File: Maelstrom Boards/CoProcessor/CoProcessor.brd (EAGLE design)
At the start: 101.6 x 101.6 mm, 51 parts, among them J1 USB_MINI-B_SMT, P1 RB1-125BAG1A, Q1 310mA/60V/1.6Ω, Q2 310mA/60V/1.6Ω, Q3 310mA/60V/1.6Ω, Q4 310mA/60V/1.6Ω, Q5 310mA/60V/1.6Ω, Q6 310mA/60V/1.6Ω, Q7 310mA/60V/1.6Ω, Q8 310mA/60V/1.6Ω, U1 W5500, U2 STM32F405RGT6, Y1 16MHz, Y2 25MHz

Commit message: continued work on copro schematic
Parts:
- added C10: 6.8nF, rcl:C0603
- added C11: 6.8 nF, rcl:C0603
- added C12: 10 nF, rcl:C0603
- added C9: 100 nF, rcl:C0603
- added R25, R26, R28, R29: 49, rcl:R0603
- added S1: MOMENTARY-SWITCH-SPST-PTH-6.0MM, SparkFun-Switches:TACTILE_SWITCH_PTH_6.0MM
- moved C5 40.2 mm to (50.9, 42.5)
- moved C6 34.9 mm to (55.9, 42.5), turned to 0 degrees
- moved R22 33.3 mm to (26.1, 42.2)
- moved R21 31.7 mm to (36.8, 50.1)
- moved C4 18.4 mm to (43.2, 31.9), turned to 180 degrees
- moved R24 16.9 mm to (61.5, 51.8)
- moved U1 16.9 mm to (46.3, 51.9)
- moved Y2 16.9 mm to (66.8, 51.8)
- moved C8 15.9 mm to (57.0, 49.6), turned to 90 degrees
- moved C7 15.7 mm to (57.0, 54.0)
- moved R20 12.7 mm to (80.5, 69.1), turned to 180 degrees
- moved R12 10.2 mm to (82.5, 74.0), turned to 180 degrees
- moved R13 8.94 mm to (82.5, 77.7), turned to 180 degrees
- moved R23 6.58 mm to (26.2, 78.7)
- moved C3 5.51 mm to (34.6, 17.0), turned to 90 degrees
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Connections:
- new net N$26: C10.2, P1.R8
- new net N$27: C11.2, P1.R7
- new net N$28: C12.1, R28.1, R29.1
- new net N$34: S1.3, U2.7
- new net SPI_RESET: U1.37, U2.25
- net +3V3: now also C9.2, P1.R3, R25.2, R26.2
- net GND: now also C12.2, C9.1, S1.1
- net N$16: now also R25.1
- net N$17: now also R26.1
- net N$18: now also C10.1, R29.2; no longer P1.R8
- net N$19: now also C11.1, R28.2; no longer P1.R7
- net SPI_MISO: now also U1.34
- net SPI_MOSI: now also U1.35
- net SPI_SCK: now also U1.33
- net SPI_SS: now also U1.32
- net USB_DN: now also U2.44
- net USB_DP: now also U2.45
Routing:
- net N$34: track 0.00 -> 62.8 mm, vias 0 -> 3
- net 5V_CNTRL: track 0.00 -> 60.2 mm, vias 0 -> 3
- net +3V3: track 157.7 -> 216.9 mm
- net 3V3_CNTRL: track 0.00 -> 49.7 mm, vias 0 -> 3
- net SW_4: track 0.00 -> 39.8 mm, vias 0 -> 2
- net SW_5: track 0.00 -> 36.6 mm
- net N$20: track 0.00 -> 28.9 mm
- net N$22: track 0.00 -> 26.8 mm
- net N$18: track 0.00 -> 24.1 mm, vias 0 -> 2
- net N$27: track 0.00 -> 21.7 mm
- net N$19: track 0.00 -> 19.4 mm
- net N$24: track 0.00 -> 19.1 mm
- net N$25: track 0.00 -> 19.1 mm
- net N$5: track 0.00 -> 18.2 mm
- net N$4: track 0.00 -> 17.0 mm
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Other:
- outline, holes or cut-outs redrawn

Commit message: ripped up parts of the board to redo
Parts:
- moved S1 107.6 mm to (-19.9, 38.2)
- moved C4 27.6 mm to (63.8, 50.3)
- moved C1 27.2 mm to (30.3, 44.8)
- moved C2 27.2 mm to (30.3, 48.5)
- moved U2 27.2 mm to (51.8, 47.0)
- moved Y1 27.2 mm to (36.9, 46.9)
- moved C3 27.0 mm to (55.1, 34.6)
- moved C9 25.5 mm to (24.8, 85.9)
- moved U1 25.5 mm to (47.1, 77.4)
- moved C11 25.5 mm to (31.8, 72.2)
- moved C12 25.5 mm to (29.3, 84.7)
- moved C5 25.5 mm to (51.7, 68.0)
- moved C6 25.5 mm to (56.7, 68.0)
- moved C7 25.5 mm to (57.8, 79.5)
- moved P1 25.5 mm to (8.50, 82.0)
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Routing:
- net PWM_3V3_CH8: track 74.6 -> 0.28 mm, vias 1 -> 0
- net PWM_3V3_CH7: track 66.6 -> 0.00 mm, vias 1 -> 0
- net PWM_3V3_CH6: track 62.9 -> 0.00 mm, vias 1 -> 0
- net N$34: track 62.8 -> 0.00 mm, vias 3 -> 0
- net 5V_CNTRL: track 60.2 -> 0.00 mm, vias 3 -> 0
- net PWM_3V3_CH5: track 55.9 -> 0.00 mm, vias 5 -> 0
- net +3V3: track 216.9 -> 166.2 mm, vias 7 -> 6
- net 3V3_CNTRL: track 49.7 -> 0.00 mm, vias 3 -> 0
- net BP_SCL: track 80.7 -> 33.0 mm, vias 2 -> 0
- net PWM_3V3_CH2: track 45.6 -> 0.07 mm, vias 3 -> 0
- net BP_SDA: track 75.6 -> 31.0 mm, vias 2 -> 0
- net SW_KILL: track 40.4 -> 0.40 mm
- net SW_4: track 39.8 -> 0.00 mm, vias 2 -> 0
- net SW_3: track 38.9 -> 0.00 mm, vias 2 -> 0
- net PWM_3V3_CH4: track 37.7 -> 0.00 mm, vias 1 -> 0
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
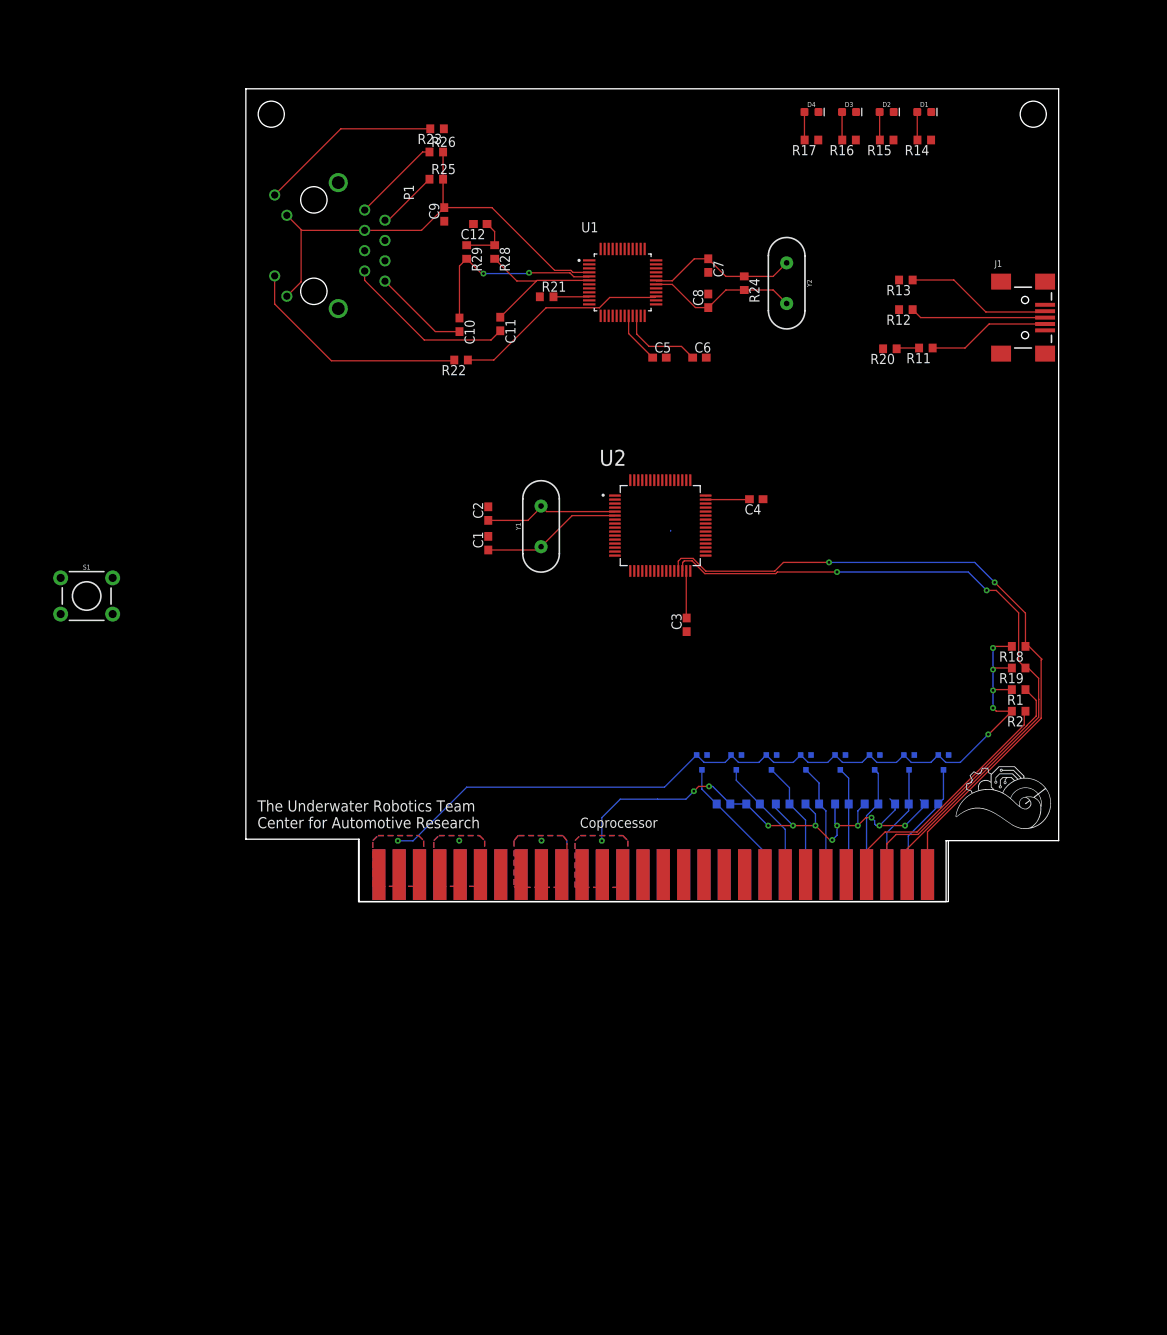
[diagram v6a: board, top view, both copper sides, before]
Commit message: finished up the initial routing on the copro board layout
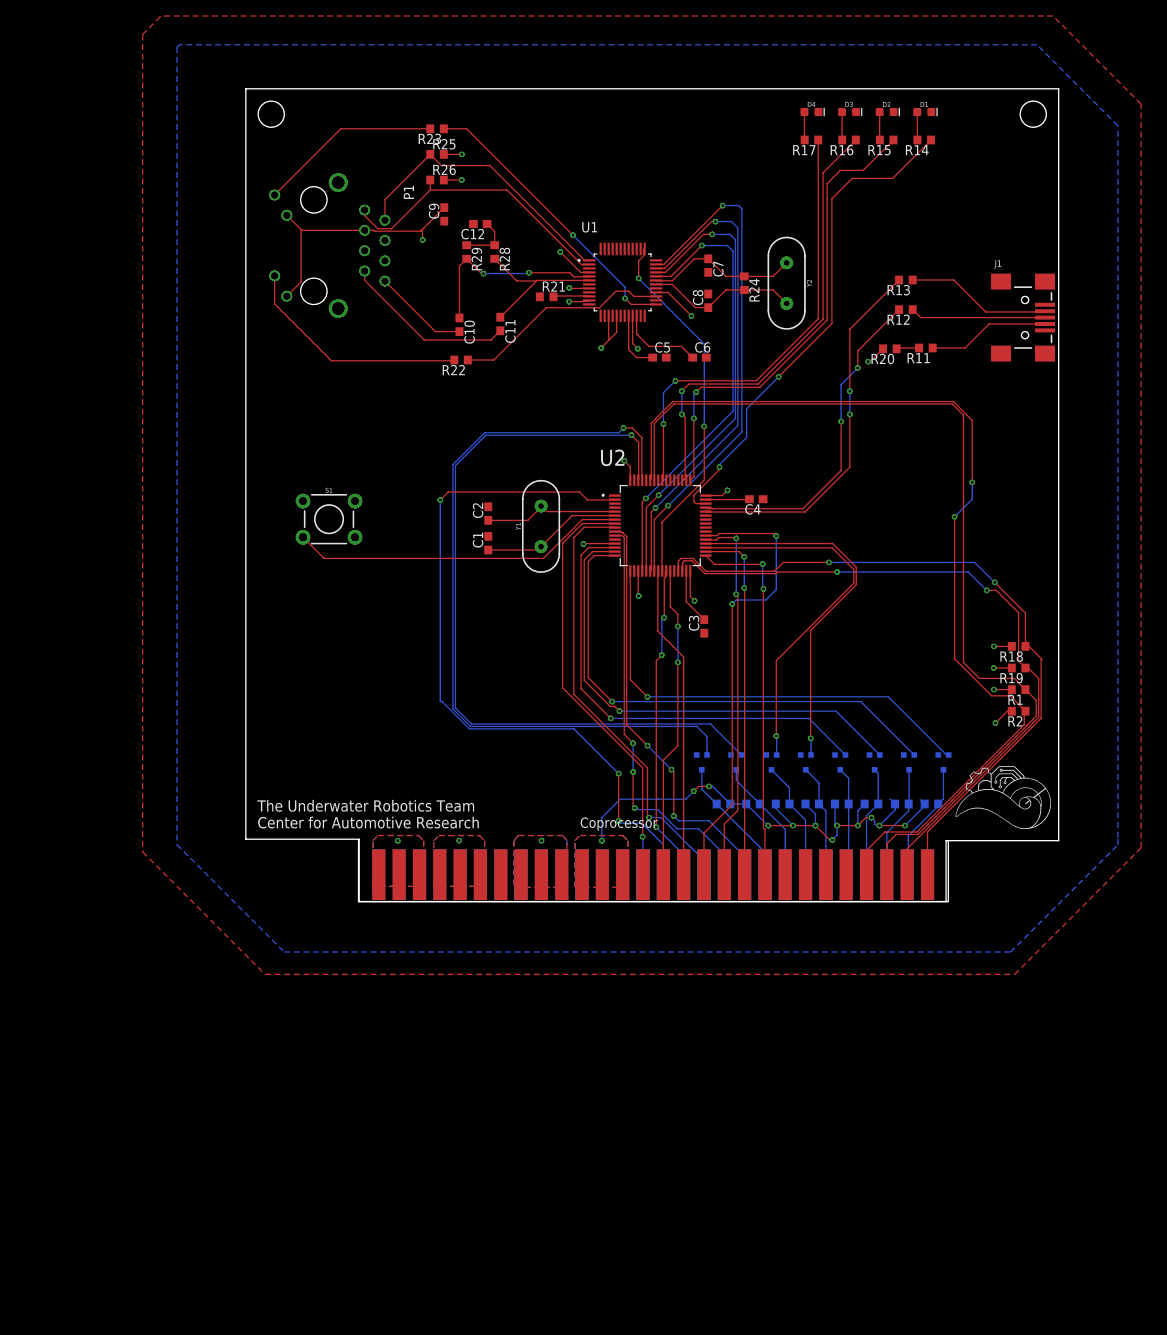
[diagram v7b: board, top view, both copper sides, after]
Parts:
- moved S1 31.8 mm to (10.4, 47.8)
- moved R26 3.50 mm to (23.9, 90.2)
- moved R25 3.10 mm to (23.9, 93.4)
- moved C3 2.21 mm to (57.3, 34.4)
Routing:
- net PWM_3V3_CH2: track 0.07 -> 98.1 mm, vias 0 -> 1
- net PWM_3V3_CH1: track 0.17 -> 97.4 mm, vias 0 -> 1
- net BP_SDA: track 31.0 -> 122.7 mm, vias 0 -> 2
- net 5V_CNTRL: track 0.00 -> 91.5 mm, vias 0 -> 3
- net BP_SCL: track 33.0 -> 120.4 mm
- net +3V3: track 166.2 -> 93.3 mm, vias 6 -> 20
- net SPI_MOSI: track 0.00 -> 63.7 mm, vias 0 -> 2
- net PWM_3V3_CH7: track 0.00 -> 62.9 mm, vias 0 -> 1
- net LED_RED: track 0.00 -> 62.0 mm, vias 0 -> 2
- net SPI_MISO: track 0.00 -> 60.4 mm, vias 0 -> 2
- net PWM_3V3_CH6: track 0.00 -> 60.1 mm, vias 0 -> 1
- net LED_YELLOW: track 0.00 -> 59.0 mm, vias 0 -> 2
- net SPI_SCK: track 0.00 -> 58.2 mm, vias 0 -> 2
- net PWM_3V3_CH5: track 0.00 -> 57.8 mm, vias 0 -> 1
- net SW_3: track 0.00 -> 57.3 mm, vias 0 -> 2
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
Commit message: changing planes for ground and power
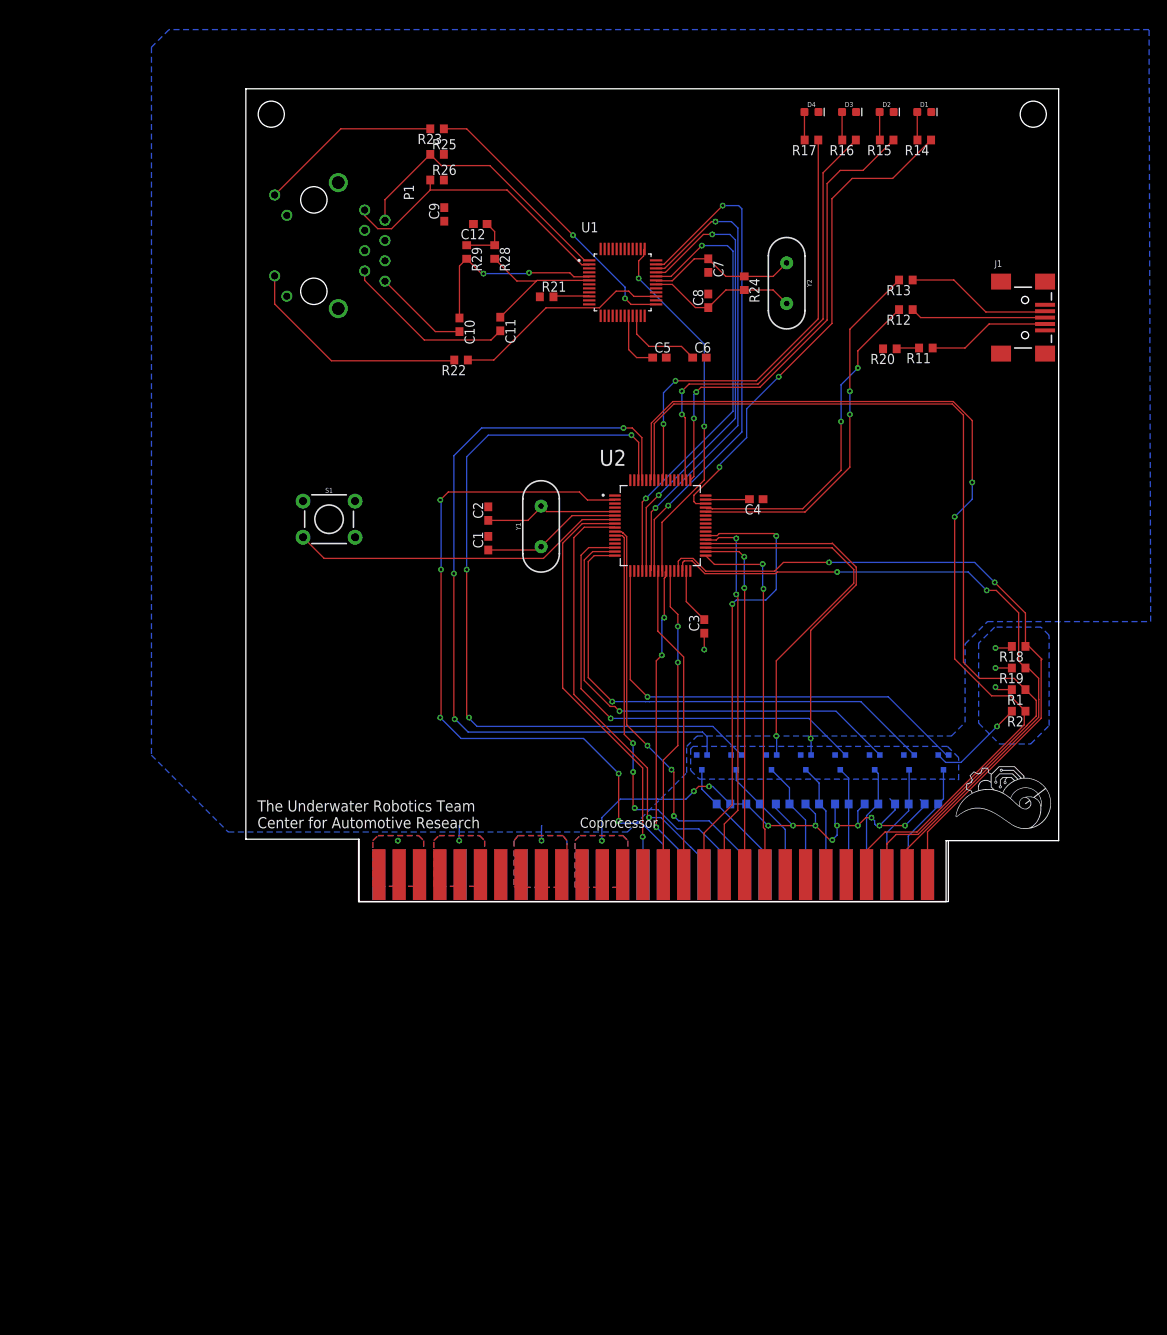
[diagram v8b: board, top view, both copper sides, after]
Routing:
- net +3V3: track 93.3 -> 18.8 mm, vias 20 -> 5
- net GND: track 0.00 -> 5.84 mm, vias 2 -> 3
- net PWM_3V3_CH2: track 98.1 -> 96.5 mm, vias 1 -> 3
- net 5V_CNTRL: track 91.5 -> 92.8 mm, vias 3 -> 5
- net PWM_3V3_CH1: track 97.4 -> 98.5 mm, vias 1 -> 3
